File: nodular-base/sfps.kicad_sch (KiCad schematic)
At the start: 6 parts, among them J1 Conn_02x10_Counter_Clockwise, J2 Conn_02x10_Counter_Clockwise, J3 Conn_02x10_Counter_Clockwise, J4 Conn_02x10_Counter_Clockwise, J5 Conn_02x10_Counter_Clockwise, J6 Conn_02x10_Counter_Clockwise

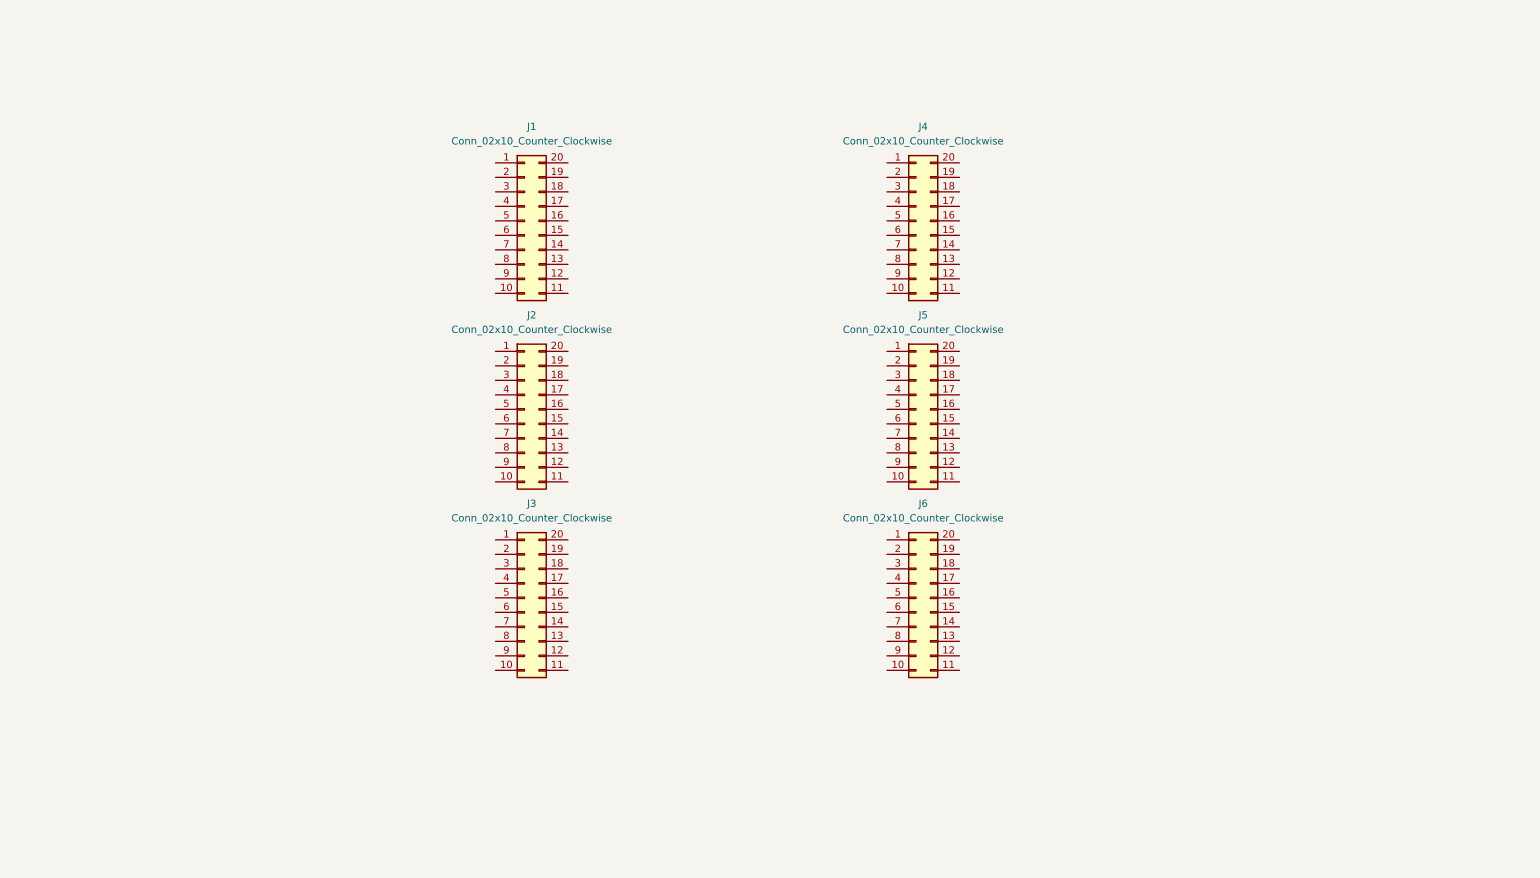
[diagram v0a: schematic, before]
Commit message: Nodular-base: Add most components onto baseboard for a test fit. Nodular-base: Add fps and models for solderable standoffs, replace solderable standoffs and reposition them. Nodule template: Adjust nodule template hole position, export STEP of nodule. Nodular-base: Add many components to schematic, structure schematic hierarchy Nodular-base: Route USB, RF path, and MCU decoupling
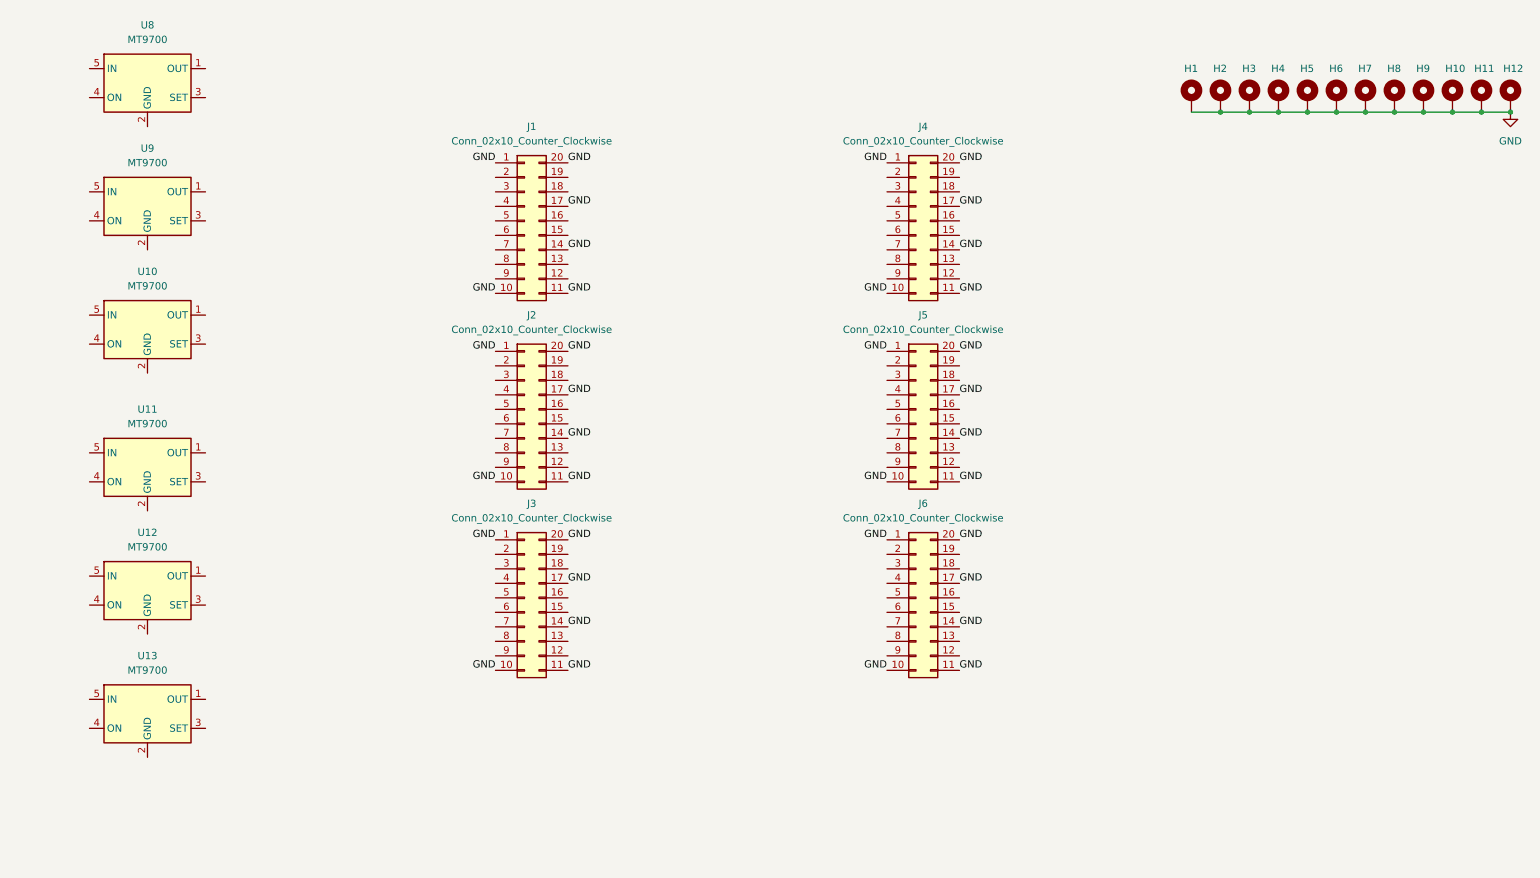
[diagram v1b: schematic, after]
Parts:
- added H1, H10, H11, H12, H2, H3, H4, H5, H6, H7, H8, H9: MountingHole_Pad, nodular:SMTSO2030CTJ, symbol Mechanical:MountingHole_Pad
- added U10, U11, U12, U13, U8, U9: MT9700, Package_TO_SOT_SMD:SOT-23-5, symbol Power_Management:AAT4610BIGV-1-T1
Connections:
- net GND: now reaches J2.1 (Pin_1)
- net GND: now also J1.1 (Pin_1), J1.10 (Pin_10), J1.11 (Pin_11), J1.14 (Pin_14), J1.17 (Pin_17), J1.20 (Pin_20), J2.10 (Pin_10), J2.11 (Pin_11), J2.14 (Pin_14), J2.17 (Pin_17), J2.20 (Pin_20), J3.1 (Pin_1), J3.10 (Pin_10), J3.11 (Pin_11), J3.14 (Pin_14), J3.17 (Pin_17), J3.20 (Pin_20), J4.1 (Pin_1), J4.10 (Pin_10), J4.11 (Pin_11), J4.14 (Pin_14), J4.17 (Pin_17), J4.20 (Pin_20), J5.1 (Pin_1), J5.10 (Pin_10), J5.11 (Pin_11), J5.14 (Pin_14), J5.17 (Pin_17), J5.20 (Pin_20), J6.1 (Pin_1), J6.10 (Pin_10), J6.11 (Pin_11), J6.14 (Pin_14), J6.17 (Pin_17), J6.20 (Pin_20), H1.1, H10.1, H11.1, H12.1, H2.1, H3.1, H4.1, H5.1, H6.1, H7.1, H8.1, H9.1

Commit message: WIP layout for base
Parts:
- added C10, C11, C12, C13, C14, C15, C17, C18, C19, C20, C21, C22: 10uF, Capacitor_SMD:C_1206_3216Metric, symbol Device:C
- added R10, R15, R18, R21, R5, R7: 10k, Resistor_SMD:R_0402_1005Metric, symbol Device:R
- added R11, R16, R19, R22, R3, R8: 11k3, Resistor_SMD:R_0402_1005Metric, symbol Device:R
- added R14, R17, R20, R4, R6, R9: 100k, Resistor_SMD:R_0402_1005Metric, symbol Device:R
- added U15, U19, U23, U31, U32, U33: 74LVC1G04, Package_TO_SOT_SMD:SOT-353_SC-70-5, symbol 74xGxx:74LVC1G04
- added U16, U17, U18, U20, U21, U22, U27, U28, U29, U34, U35, U36, U37, U38, U39, U40, U41, U42: RCLAMP0524P-ES, Package_DFN_QFN:Diodes_UDFN-10_1.0x2.5mm_P0.5mm, symbol nodular:RCLAMP0524P-ES
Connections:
- net GND: now also U10.2 (GND), U11.2 (GND), U12.2 (GND), U13.2 (GND), U8.2 (GND), U9.2 (GND), C10.2, C11.2, C12.2, C13.2, C14.2, C15.2, C17.2, C18.2, C19.2, C20.2, C21.2, C22.2, R11.2, R16.2, R19.2, R22.2, R3.2, R8.2, U15.3 (GND), U16.3 (GND), U16.8 (GND), U17.3 (GND), U17.8 (GND), U18.3 (GND), U18.8 (GND), U19.3 (GND), U20.3 (GND), U20.8 (GND), U21.3 (GND), U21.8 (GND), U22.3 (GND), U22.8 (GND), U23.3 (GND), U27.3 (GND), U27.8 (GND), U28.3 (GND), U28.8 (GND), U29.3 (GND), U29.8 (GND), U31.3 (GND), U32.3 (GND), U33.3 (GND), U34.3 (GND), U34.8 (GND), U35.3 (GND), U35.8 (GND), U36.3 (GND), U36.8 (GND), U37.3 (GND), U37.8 (GND), U38.3 (GND), U38.8 (GND), U39.3 (GND), U39.8 (GND), U40.3 (GND), U40.8 (GND), U41.3 (GND), U41.8 (GND), U42.3 (GND), U42.8 (GND)
- net BH1: now reaches J2.12 (Pin_12)
- net BH1: now also U20.5 (CHD), U20.6 (CHD)
- net BH2: now reaches J2.13 (Pin_13)
- net BH2: now also U20.4 (CHC), U20.7 (CHC)
- net PORTB_3V3: now reaches J2.15 (Pin_15)
- net PORTB_3V3: now also J2.16 (Pin_16), U9.1 (OUT), C13.1
- net BH3: now reaches J2.18 (Pin_18)
- net BH3: now also U20.2 (CHB), U20.9 (CHB)
- net BH4: now reaches J2.19 (Pin_19)
- net BH4: now also U20.1 (CHA), U20.10 (CHA)
- net BLS1: now reaches J2.2 (Pin_2)
- net BLS1: now also U21.1 (CHA), U21.10 (CHA)
- net BLS2: now reaches J2.3 (Pin_3)
- net BLS2: now also U21.2 (CHB), U21.9 (CHB)
- net SDA_B: now reaches J2.4 (Pin_4)
- net SDA_B: now also U21.4 (CHC), U21.7 (CHC)
- net SCL_B: now reaches J2.5 (Pin_5)
- net SCL_B: now also U21.5 (CHD), U21.6 (CHD)
- net B_NDET: now reaches J2.6 (Pin_6)
- net B_NDET: now also R7.2, U22.1 (CHA), U22.10 (CHA)
- net BLS3: now reaches J2.7 (Pin_7)
- net BLS3: now also U22.2 (CHB), U22.9 (CHB)
- net BLS4: now reaches J2.8 (Pin_8)
- net BLS4: now also U22.4 (CHC), U22.7 (CHC)
- net BLS5: now reaches J2.9 (Pin_9)
- net BLS5: now also U22.5 (CHD), U22.6 (CHD)
- net EH1: now reaches J5.12 (Pin_12)
- net EH1: now also U39.5 (CHD), U39.6 (CHD)
- net EH2: now reaches J5.13 (Pin_13)
- net EH2: now also U39.4 (CHC), U39.7 (CHC)
- net PORTE_3V3: now reaches J5.15 (Pin_15)
- net PORTE_3V3: now also J5.16 (Pin_16), U12.1 (OUT), C20.1
- net EH3: now reaches J5.18 (Pin_18)
- net EH3: now also U39.2 (CHB), U39.9 (CHB)
- net EH4: now reaches J5.19 (Pin_19)
- net EH4: now also U39.1 (CHA), U39.10 (CHA)
- net ELS1: now reaches J5.2 (Pin_2)
- net ELS1: now also U37.1 (CHA), U37.10 (CHA)
- net ELS2: now reaches J5.3 (Pin_3)
- net ELS2: now also U37.2 (CHB), U37.9 (CHB)
- net SDA_E: now reaches J5.4 (Pin_4)
- net SDA_E: now also U37.4 (CHC), U37.7 (CHC)
- net SCL_E: now reaches J5.5 (Pin_5)
- net SCL_E: now also U37.5 (CHD), U37.6 (CHD)
- net E_NDET: now reaches J5.6 (Pin_6)
- net E_NDET: now also R18.2, U38.1 (CHA), U38.10 (CHA)
- net ELS3: now reaches J5.7 (Pin_7)
- net ELS3: now also U38.2 (CHB), U38.9 (CHB)
- net ELS4: now reaches J5.8 (Pin_8)
- net ELS4: now also U38.4 (CHC), U38.7 (CHC)
- net ELS5: now reaches J5.9 (Pin_9)
- net ELS5: now also U38.5 (CHD), U38.6 (CHD)
- net AH1: now reaches J1.12 (Pin_12)
- net AH1: now also U16.5 (CHD), U16.6 (CHD)
- net AH2: now reaches J1.13 (Pin_13)
- net AH2: now also U16.4 (CHC), U16.7 (CHC)
- net PORTA_3V3: now reaches J1.15 (Pin_15)
- net PORTA_3V3: now also J1.16 (Pin_16), U8.1 (OUT), C10.1
- net AH3: now reaches J1.18 (Pin_18)
- net AH3: now also U16.2 (CHB), U16.9 (CHB)
- net AH4: now reaches J1.19 (Pin_19)
- net AH4: now also U16.1 (CHA), U16.10 (CHA)
- net ALS1: now reaches J1.2 (Pin_2)
- net ALS1: now also U17.1 (CHA), U17.10 (CHA)
- net ALS2: now reaches J1.3 (Pin_3)
- net ALS2: now also U17.2 (CHB), U17.9 (CHB)
- net SDA_A: now reaches J1.4 (Pin_4)
- net SDA_A: now also U17.4 (CHC), U17.7 (CHC)
- net SCL_A: now reaches J1.5 (Pin_5)
- net SCL_A: now also U17.5 (CHD), U17.6 (CHD)
- net A_NDET: now reaches J1.6 (Pin_6)
- net A_NDET: now also R5.2, U18.1 (CHA), U18.10 (CHA)
- net ALS3: now reaches J1.7 (Pin_7)
- net ALS3: now also U18.2 (CHB), U18.9 (CHB)
- net ALS4: now reaches J1.8 (Pin_8)
- net ALS4: now also U18.4 (CHC), U18.7 (CHC)
- net ALS5: now reaches J1.9 (Pin_9)
- net ALS5: now also U18.5 (CHD), U18.6 (CHD)
- net DH1: now reaches J4.12 (Pin_12)
- net DH1: now also U36.5 (CHD), U36.6 (CHD)
- net DH2: now reaches J4.13 (Pin_13)
- net DH2: now also U36.4 (CHC), U36.7 (CHC)
- net PORTD_3V3: now reaches J4.15 (Pin_15)
- net PORTD_3V3: now also J4.16 (Pin_16), U11.1 (OUT), C18.1
- net DH3: now reaches J4.18 (Pin_18)
- net DH3: now also U36.2 (CHB), U36.9 (CHB)
- net DH4: now reaches J4.19 (Pin_19)
- net DH4: now also U36.1 (CHA), U36.10 (CHA)
- net DLS1: now reaches J4.2 (Pin_2)
- net DLS1: now also U34.1 (CHA), U34.10 (CHA)
- net DLS2: now reaches J4.3 (Pin_3)
- net DLS2: now also U34.2 (CHB), U34.9 (CHB)
- net SDA_D: now reaches J4.4 (Pin_4)
- net SDA_D: now also U34.4 (CHC), U34.7 (CHC)
- net SCL_D: now reaches J4.5 (Pin_5)
- net SCL_D: now also U34.5 (CHD), U34.6 (CHD)
- net D_NDET: now reaches J4.6 (Pin_6)
- net D_NDET: now also R15.2, U35.1 (CHA), U35.10 (CHA)
- net DLS3: now reaches J4.7 (Pin_7)
- net DLS3: now also U35.2 (CHB), U35.9 (CHB)
- net DLS4: now reaches J4.8 (Pin_8)
- net DLS4: now also U35.4 (CHC), U35.7 (CHC)
- net DLS5: now reaches J4.9 (Pin_9)
- net DLS5: now also U35.5 (CHD), U35.6 (CHD)
- net at U11.3 (SET): now also R16.1
- net D_LSEN: now reaches U11.4 (ON)
- net D_LSEN: now also U31.4
- net 3V3_SYS: now reaches U11.5 (IN)
- net 3V3_SYS: now also U10.5 (IN), U12.5 (IN), U13.5 (IN), U8.5 (IN), U9.5 (IN), C11.1, C12.1, C14.1, C17.1, C19.1, C21.1, R14.1, R17.1, R20.1, R4.1, R6.1, R9.1, U15.5 (VCC), U19.5 (VCC), U23.5 (VCC), U31.5 (VCC), U32.5 (VCC), U33.5 (VCC)
- net CH1: now reaches J3.12 (Pin_12)
- net CH1: now also U29.5 (CHD), U29.6 (CHD)
- net CH2: now reaches J3.13 (Pin_13)
- net CH2: now also U29.4 (CHC), U29.7 (CHC)
- net PORTC_3V3: now reaches J3.15 (Pin_15)
- net PORTC_3V3: now also J3.16 (Pin_16), U10.1 (OUT), C15.1
- net CH3: now reaches J3.18 (Pin_18)
- net CH3: now also U29.2 (CHB), U29.9 (CHB)
- net CH4: now reaches J3.19 (Pin_19)
- net CH4: now also U29.1 (CHA), U29.10 (CHA)
- net CLS1: now reaches J3.2 (Pin_2)
- net CLS1: now also U27.1 (CHA), U27.10 (CHA)
- net CLS2: now reaches J3.3 (Pin_3)
- net CLS2: now also U27.2 (CHB), U27.9 (CHB)
- net SDA_C: now reaches J3.4 (Pin_4)
- net SDA_C: now also U27.4 (CHC), U27.7 (CHC)
- net SCL_C: now reaches J3.5 (Pin_5)
- net SCL_C: now also U27.5 (CHD), U27.6 (CHD)
- net C_NDET: now reaches J3.6 (Pin_6)
- net C_NDET: now also R10.2, U28.1 (CHA), U28.10 (CHA)
- net CLS3: now reaches J3.7 (Pin_7)
- net CLS3: now also U28.2 (CHB), U28.9 (CHB)
- net CLS4: now reaches J3.8 (Pin_8)
- net CLS4: now also U28.4 (CHC), U28.7 (CHC)
- net CLS5: now reaches J3.9 (Pin_9)
- net CLS5: now also U28.5 (CHD), U28.6 (CHD)
- net at U9.3 (SET): now also R8.1
- net B_LSEN: now reaches U9.4 (ON)
- net B_LSEN: now also U19.4
- net at U12.3 (SET): now also R19.1
- net E_LSEN: now reaches U12.4 (ON)
- net E_LSEN: now also U32.4
- net at U8.3 (SET): now also R3.1
- net A_LSEN: now reaches U8.4 (ON)
- net A_LSEN: now also U15.4
- net at U10.3 (SET): now also R11.1
- net C_LSEN: now reaches U10.4 (ON)
- net C_LSEN: now also U23.4
- net FH1: now reaches J6.12 (Pin_12)
- net FH1: now also U42.5 (CHD), U42.6 (CHD)
- net FH2: now reaches J6.13 (Pin_13)
- net FH2: now also U42.4 (CHC), U42.7 (CHC)
- net PORTF_3V3: now reaches J6.15 (Pin_15)
- net PORTF_3V3: now also J6.16 (Pin_16), U13.1 (OUT), C22.1
- net FH3: now reaches J6.18 (Pin_18)
- net FH3: now also U42.2 (CHB), U42.9 (CHB)
- net FH4: now reaches J6.19 (Pin_19)
- net FH4: now also U42.1 (CHA), U42.10 (CHA)
- net FLS1: now reaches J6.2 (Pin_2)
- net FLS1: now also U40.1 (CHA), U40.10 (CHA)
- net FLS2: now reaches J6.3 (Pin_3)
- net FLS2: now also U40.2 (CHB), U40.9 (CHB)
- net SDA_F: now reaches J6.4 (Pin_4)
- net SDA_F: now also U40.4 (CHC), U40.7 (CHC)
- net SCL_F: now reaches J6.5 (Pin_5)
- net SCL_F: now also U40.5 (CHD), U40.6 (CHD)
- net F_NDET: now reaches J6.6 (Pin_6)
- net F_NDET: now also R21.2, U41.1 (CHA), U41.10 (CHA)
- net FLS3: now reaches J6.7 (Pin_7)
- net FLS3: now also U41.2 (CHB), U41.9 (CHB)
- net FLS4: now reaches J6.8 (Pin_8)
- net FLS4: now also U41.4 (CHC), U41.7 (CHC)
- net FLS5: now reaches J6.9 (Pin_9)
- net FLS5: now also U41.5 (CHD), U41.6 (CHD)
- net at U13.3 (SET): now also R22.1
- net F_LSEN: now reaches U13.4 (ON)
- net F_LSEN: now also U33.4
- new net ND_PS_A: R4.2, R5.1, U15.2
- new net ND_PS_B: R6.2, R7.1, U19.2
- new net ND_PS_C: R10.1, R9.2, U23.2
- new net ND_PS_D: R14.2, R15.1, U31.2
- new net ND_PS_E: R17.2, R18.1, U32.2
- new net ND_PS_F: R20.2, R21.1, U33.2
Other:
- moved on the sheet: J1, J2, J3, J4, J5, J6, U10, U11, U12, U13, U8, U9

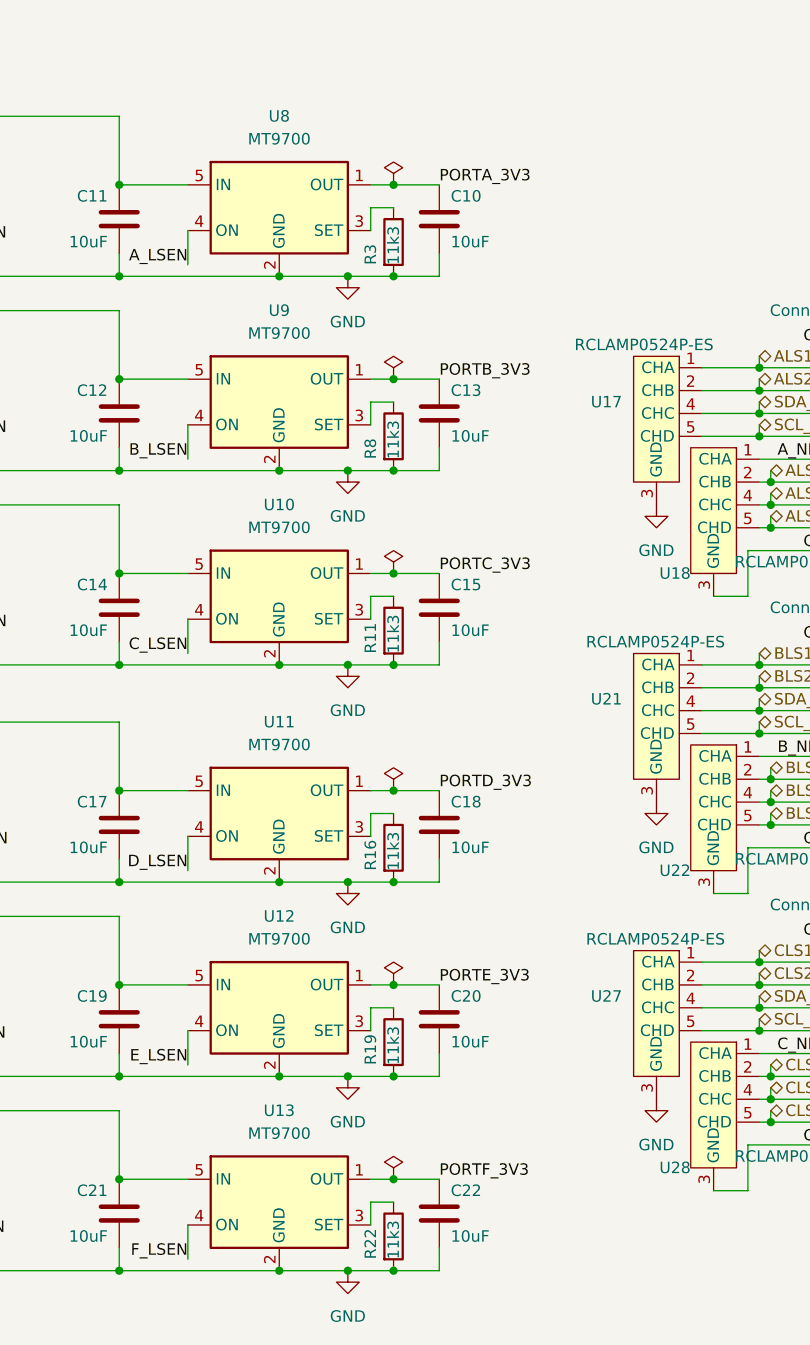
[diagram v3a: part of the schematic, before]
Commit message: Add 3d models and fix erc errors
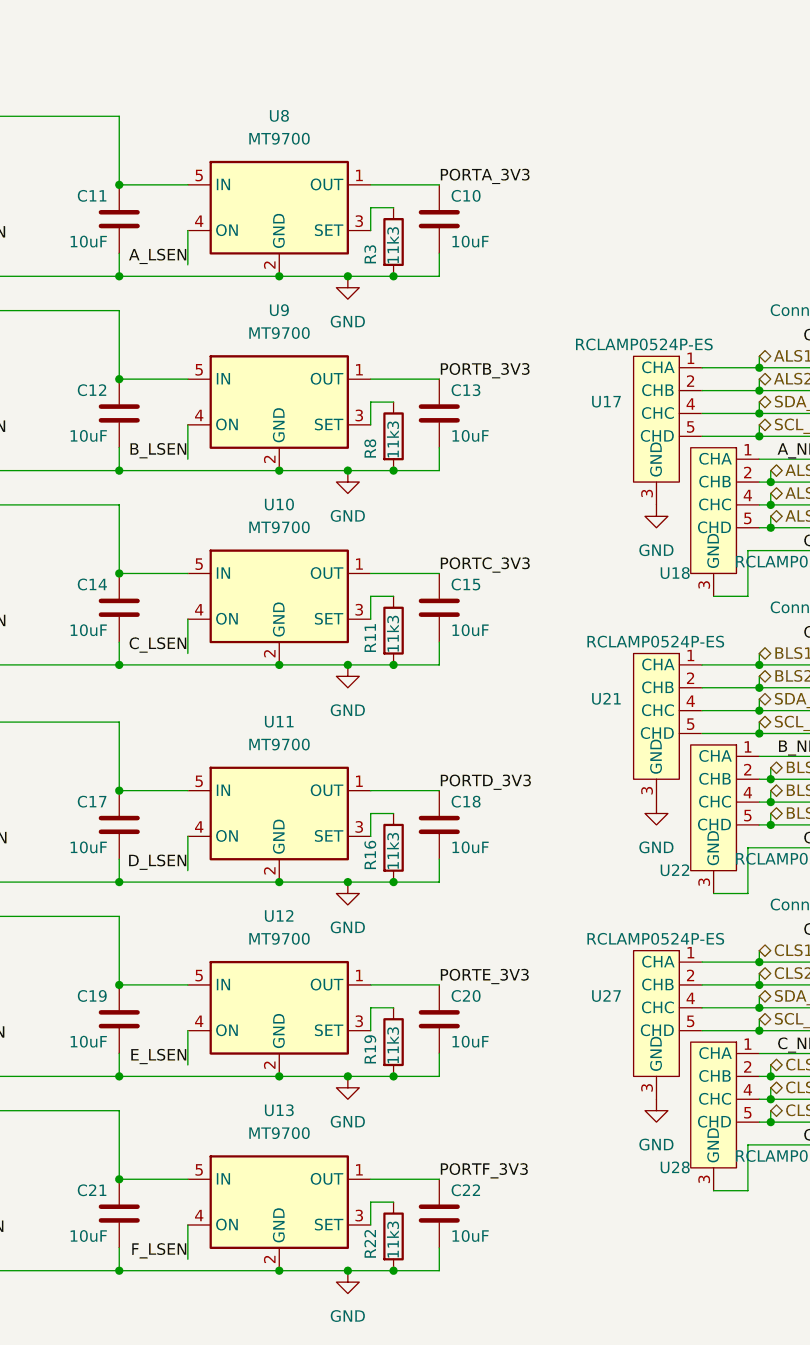
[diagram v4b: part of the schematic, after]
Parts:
- U16, U17, U18, U20, U21, U22, U27, U28, U29, U34, U35, U36, U37, U38, U39, U40, U41, U42: footprint Package_DFN_QFN:Diodes_UDFN-10_1.0x2.5mm_P0.5mm -> nodular:Diodes_UDFN-10_1.0x2.5mm_P0.5mm
